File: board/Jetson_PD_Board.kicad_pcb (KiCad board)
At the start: 2 copper layers, 23.8 x 42.2 mm, 47 parts, among them J1 USB4081-03-A, J2 768250002, Q1 NTTFS5C673NLTAG, Q2 NTTFS5C673NLTAG, Q3 NTTFS5C673NLTAG, U1 APK43070DKZ-13-FA01, U2 USBLC6-2SC6

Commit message: Finished new layout before routing
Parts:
- moved D5 49.8 mm to (132.7, 79.8), turned to 180 degrees
- moved R12 49.6 mm to (129.5, 79.8), turned to 0 degrees
- moved U2 49.6 mm to (117.5, 105.8), turned to 0 degrees
- moved R1 47.3 mm to (129.4, 81.2), turned to 0 degrees
- moved C6 39.2 mm to (129.2, 99.0)
- moved R11 32.4 mm to (129.6, 105.8), turned to 0 degrees
- moved C9 31.2 mm to (121.5, 105.2)
- moved D4 30.6 mm to (132.8, 105.8), turned to 180 degrees
- moved R13 11.2 mm to (129.8, 92.0), turned to 90 degrees
- moved R16 6.57 mm to (123.2, 105.8)
- moved R17 6.57 mm to (125.0, 105.8)
- moved D1 4.69 mm to (121.5, 89.0), turned to 180 degrees
- moved C14 0.09 mm to (118.2, 99.0)
- moved R10 0.09 mm to (127.8, 92.0)
- moved R2 0.08 mm to (123.8, 92.0)
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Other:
- board size 23.8 x 42.2 mm -> 23.8 x 45.5 mm

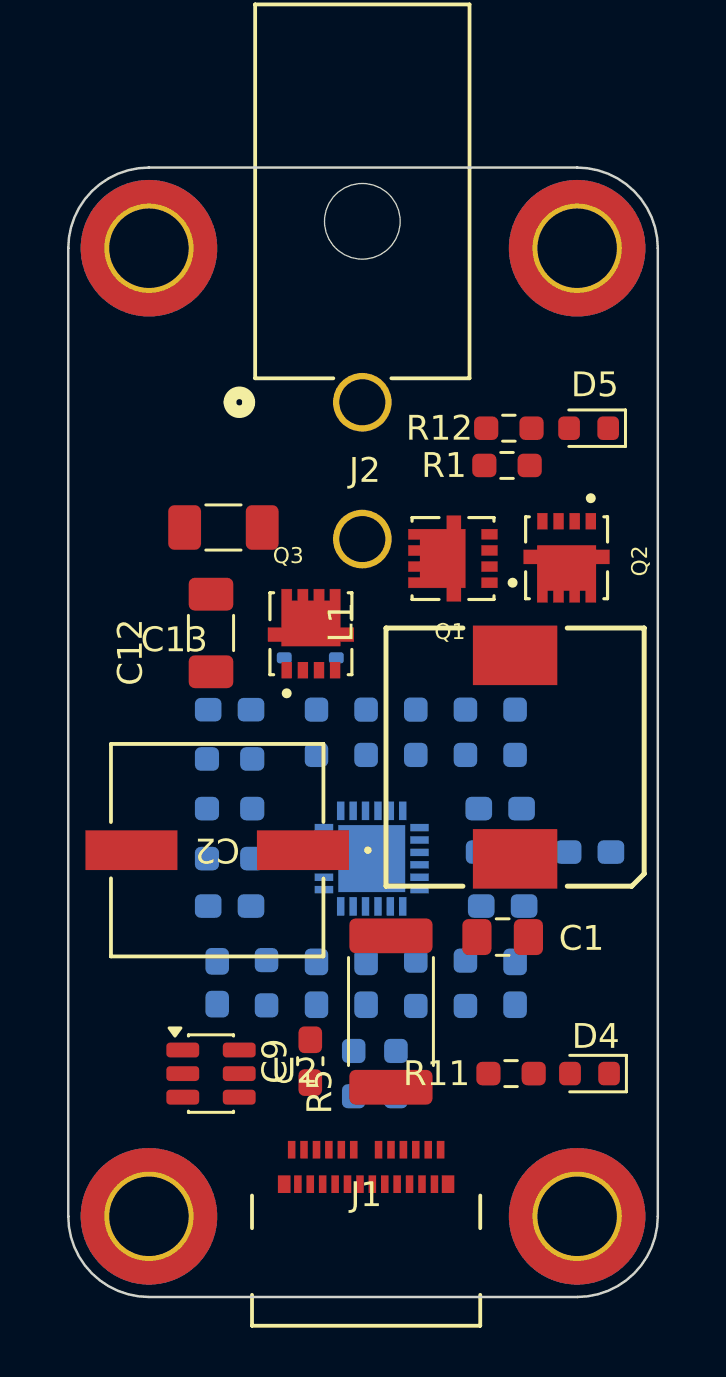
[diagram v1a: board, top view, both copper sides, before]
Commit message: Started routing power planes
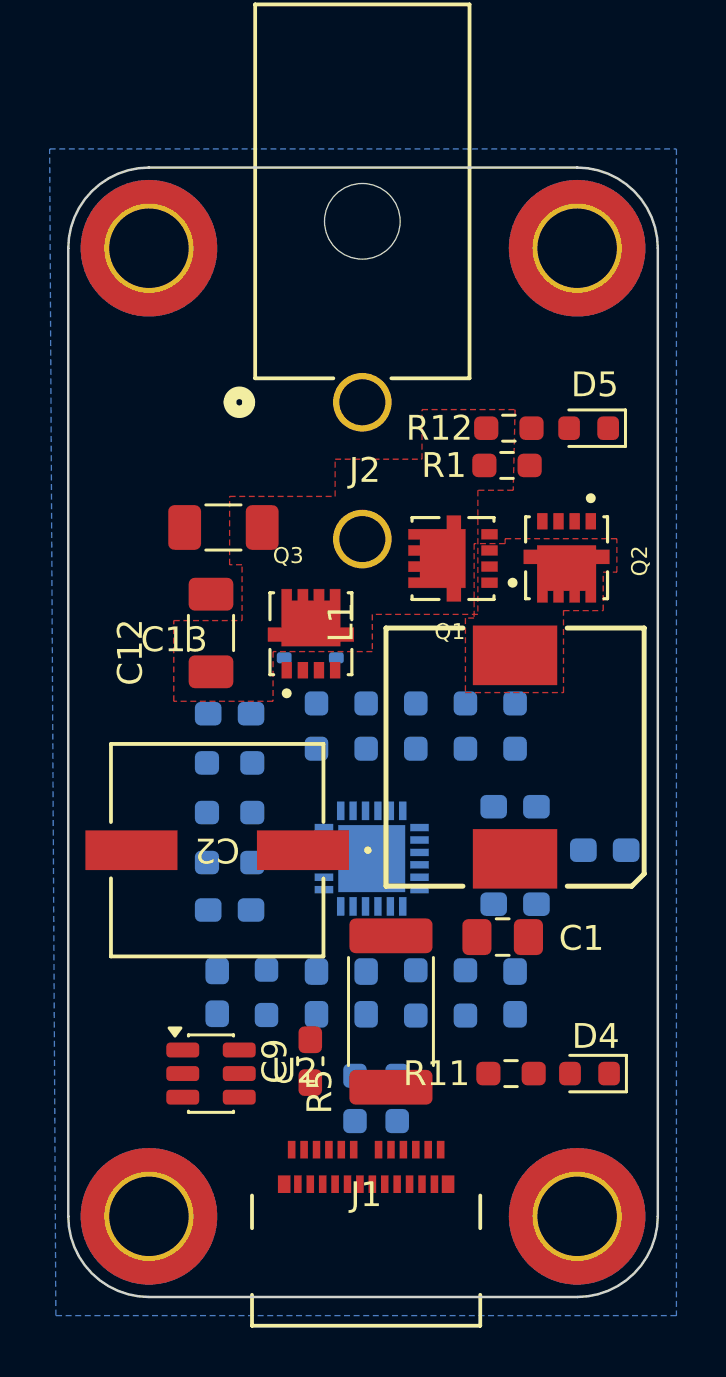
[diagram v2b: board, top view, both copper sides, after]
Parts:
- moved R16 1.00 mm to (123.3, 106.8)
- moved R17 1.00 mm to (125.0, 106.8)
- moved C3 0.62 mm to (133.4, 96.8)
- moved C4 0.60 mm to (129.8, 95.0)
- moved R4 0.59 mm to (129.8, 96.8)
- moved C6 0.51 mm to (129.8, 98.9)
- moved C10 0.39 mm to (121.8, 102.5)
- moved C5 0.39 mm to (117.8, 102.5)
- moved C7 0.39 mm to (129.8, 102.5)
- moved C8 0.39 mm to (123.8, 102.5)
- moved R3 0.39 mm to (119.7, 102.5)
- moved R6 0.39 mm to (125.8, 102.5)
- moved R7 0.39 mm to (127.8, 102.5)
- moved R10 0.25 mm to (127.8, 91.8)
- moved R13 0.25 mm to (129.8, 91.8)
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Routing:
- added copper zone on F.Cu, net /Switching_Node
- added copper zone on B.Cu, net GND
- added copper zone on F.Cu, net V_{batt}
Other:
- copper layers 2 -> 4

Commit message: aaaaaaaaaaaaaaaaaaaaaaaaA
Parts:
- C10: moved to F.Cu
- moved C10 9.09 mm to (129.5, 107.2), turned to 0 degrees
- moved C12 1.66 mm to (117.0, 86.4), turned to 180 degrees
- moved C13 1.42 mm to (118.8, 82.5), turned to 90 degrees
- moved C14 0.54 mm to (118.2, 99.7)
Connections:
- net Net-(D1-A) renamed /Buck_{out}
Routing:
- net Net-(Q2-G): track 0.00 -> 25.9 mm, vias 0 -> 2
- net Net-(U1-CC2): track 0.00 -> 23.1 mm
- net Net-(Q1-G): track 0.00 -> 20.9 mm, vias 0 -> 3
- net Net-(U1-CC1): track 0.00 -> 19.3 mm
- net Net-(U1-TS): track 0.00 -> 5.97 mm
- net CC2: track 0.00 -> 5.44 mm, vias 0 -> 1
- net Net-(U1-GPIO2): track 0.00 -> 4.70 mm
- net Net-(U1-DP): track 0.00 -> 3.34 mm
- net V_{batt}: track 0.00 -> 3.28 mm
- net Net-(U1-DN): track 0.00 -> 3.06 mm
- net Net-(D5-A): track 0.00 -> 3.04 mm
- net V_{out}: track 0.00 -> 2.98 mm
- net Net-(D4-A): track 0.00 -> 1.46 mm
- net GND: vias 0 -> 2
- added copper zone on F.Cu, net /Buck_{out}
- added copper zone on F.Cu, net GND
- added copper zone on F.Cu, net V_{out}

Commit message: Trace routing!
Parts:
- D1: moved to F.Cu
- moved R13 11.7 mm to (118.2, 89.5), turned to 0 degrees
- moved R6 10.7 mm to (122.0, 92.5)
- moved R7 10.7 mm to (124.0, 92.5)
- moved R3 10.3 mm to (130.0, 103.2)
- moved C5 10.3 mm to (128.0, 103.2)
- moved C7 5.74 mm to (124.0, 103.2)
- moved R2 4.27 mm to (128.0, 92.5)
- moved R8 4.27 mm to (126.0, 92.5)
- moved R10 4.27 mm to (131.9, 92.5)
- moved R9 4.27 mm to (129.9, 92.5)
- moved C14 3.84 mm to (121.5, 101.8), turned to -90 degrees
- moved C8 2.36 mm to (126.0, 103.2)
- moved D1 2.20 mm to (122.2, 91.1)
- moved D5 0.50 mm to (132.8, 80.2)
- moved R1 0.26 mm to (129.5, 81.0)
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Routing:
- net Net-(Q2-G): track 25.9 -> 0.00 mm, vias 2 -> 0
- net Net-(Q1-G): track 20.9 -> 0.00 mm, vias 3 -> 0
- net V_{batt}: track 3.28 -> 18.3 mm, vias 0 -> 1
- net Net-(U1-CC1): track 19.3 -> 11.1 mm
- net Net-(U1-CC2): track 23.1 -> 15.1 mm
- net Net-(D1-K): track 0.00 -> 5.34 mm, vias 0 -> 1
- net Net-(D5-A): track 3.04 -> 3.83 mm
- net GND: vias 2 -> 3

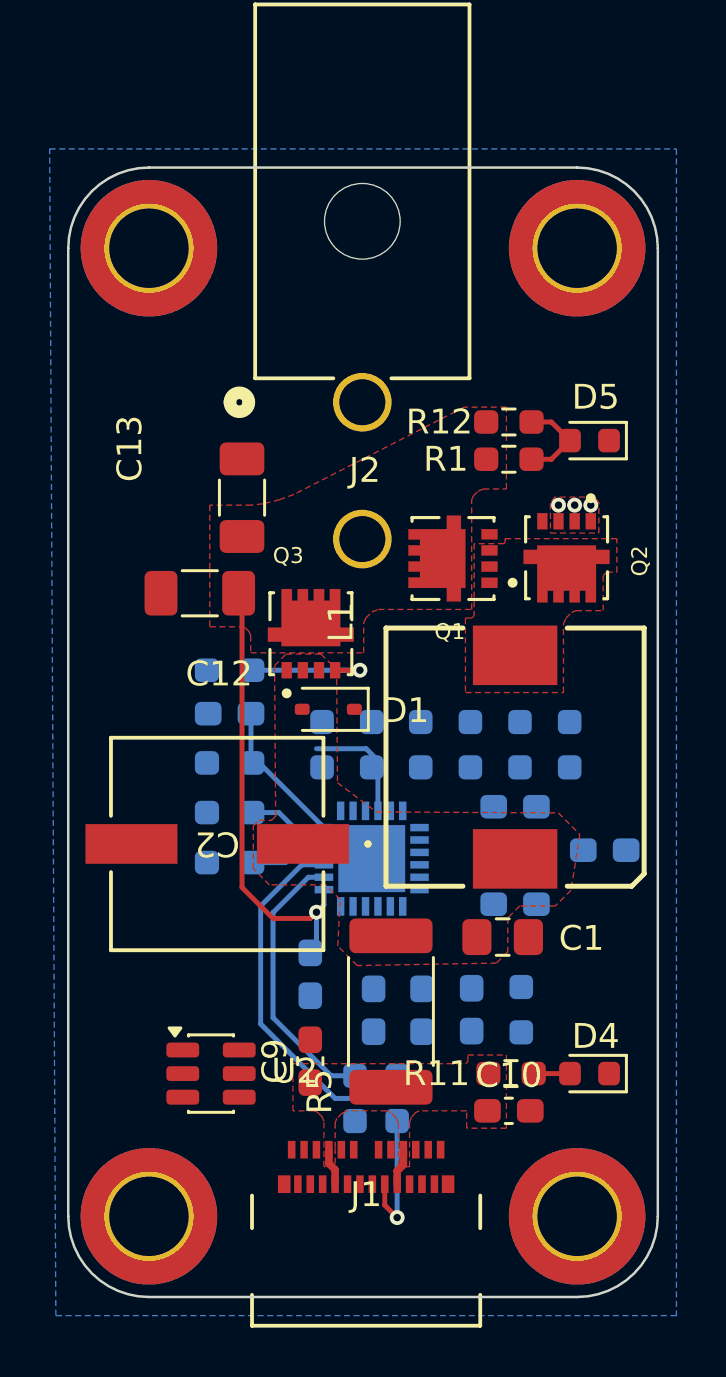
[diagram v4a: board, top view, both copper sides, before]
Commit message: Place components for a new arrangement for control IC
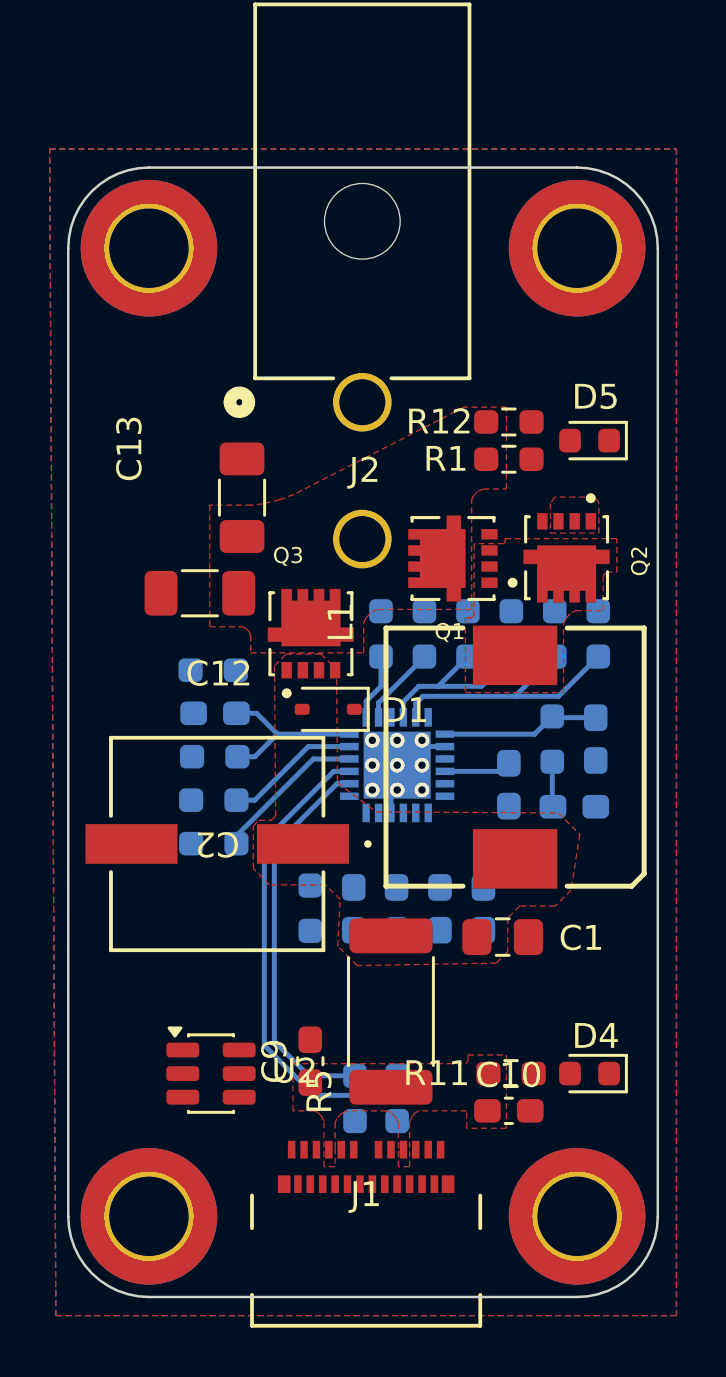
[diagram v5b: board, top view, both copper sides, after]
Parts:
- moved R3 9.43 mm to (121.5, 99.1)
- moved R6 5.06 mm to (124.3, 88.0)
- moved R7 4.94 mm to (126.1, 88.0)
- moved R8 4.85 mm to (127.8, 88.0)
- moved C6 4.82 mm to (129.5, 94.1), turned to -90 degrees
- moved R2 4.76 mm to (129.6, 88.0)
- moved R4 4.72 mm to (131.2, 92.3), turned to -90 degrees
- moved R9 4.68 mm to (131.3, 88.0)
- moved R10 4.61 mm to (133.1, 88.0)
- moved C4 4.24 mm to (133.0, 92.3), turned to -90 degrees
- moved C7 4.19 mm to (125.0, 99.1)
- moved C8 4.15 mm to (126.7, 99.1)
- moved C5 4.09 mm to (128.5, 99.1)
- moved U1 3.90 mm to (125.0, 93.3)
- moved C14 3.17 mm to (123.2, 99.1)
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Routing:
- net V_{batt}: track 18.3 -> 0.00 mm, vias 1 -> 0
- net Net-(U1-GPIO3): track 0.00 -> 11.0 mm
- net Net-(U1-COMP): track 0.00 -> 6.39 mm
- net CC2: track 5.44 -> 0.00 mm, vias 1 -> 0
- net Net-(D1-K): track 5.34 -> 0.00 mm, vias 1 -> 0
- net Net-(U1-CC1): track 11.1 -> 15.7 mm
- net Net-(U1-CC2): track 15.1 -> 19.3 mm
- net Net-(D5-A): track 3.83 -> 0.00 mm
- net Net-(U1-SCL): track 0.00 -> 3.22 mm
- net Net-(U1-DN): track 3.06 -> 6.14 mm
- net V_{out}: track 2.98 -> 0.00 mm
- net Net-(U1-GPIO2): track 4.70 -> 7.43 mm
- net /Switching_Node: track 0.00 -> 2.71 mm
- net Net-(U1-SDA): track 0.00 -> 2.70 mm
- net Net-(U1-DP): track 3.34 -> 5.44 mm
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- added copper zone on In1.Cu, net GND

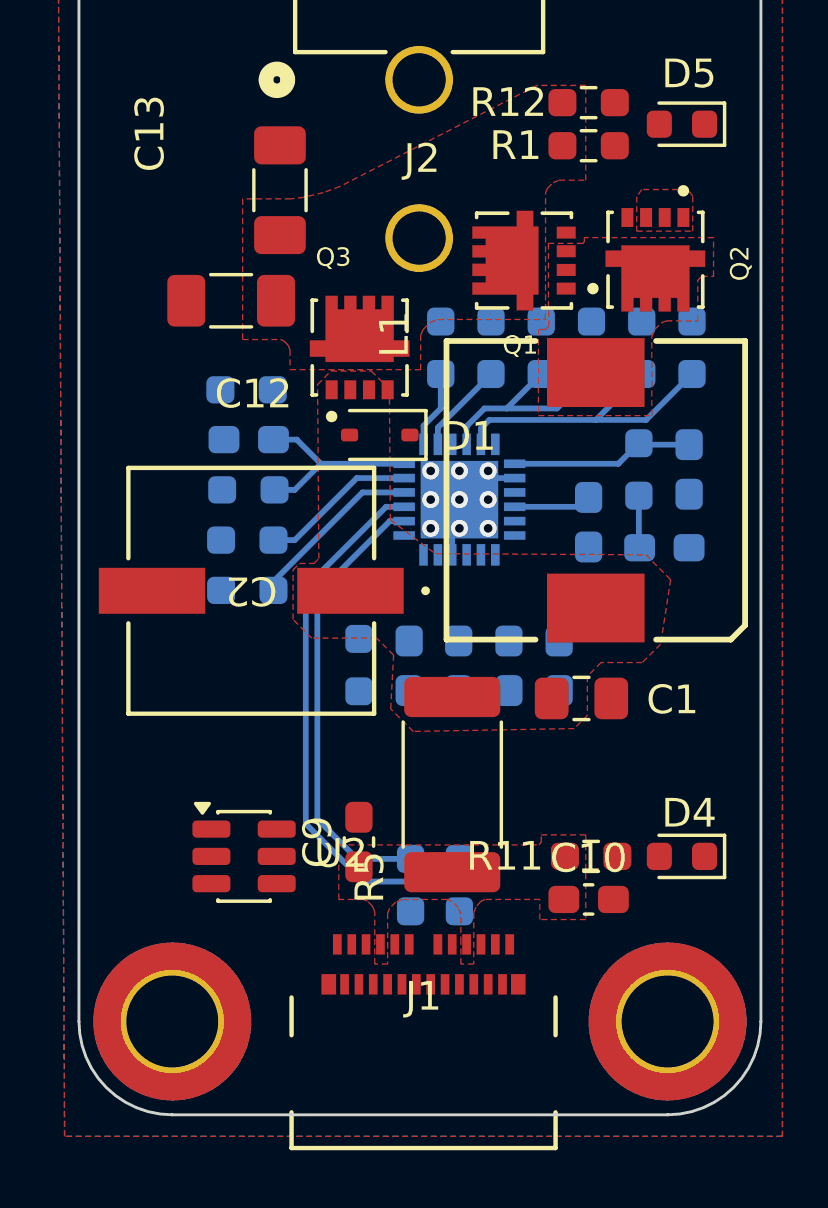
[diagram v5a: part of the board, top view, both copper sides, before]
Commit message: More trace routing
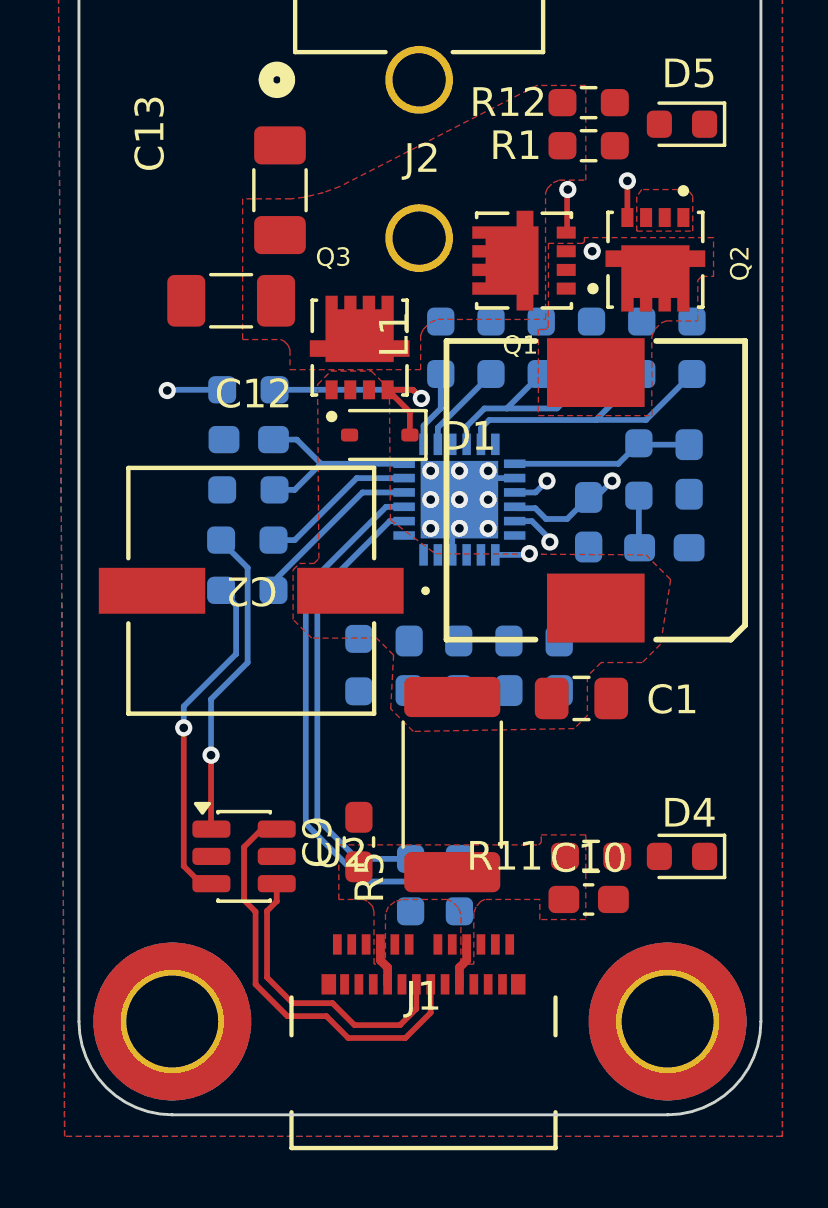
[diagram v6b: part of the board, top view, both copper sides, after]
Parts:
- moved R13 0.06 mm to (117.7, 89.5)
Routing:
- net Net-(Q1-G): track 0.00 -> 27.5 mm, vias 0 -> 2
- net /Switching_Node: track 2.71 -> 25.0 mm, vias 0 -> 2
- net Net-(U1-GATE): track 0.00 -> 20.5 mm, vias 0 -> 2
- net Net-(Q2-G): track 0.00 -> 20.4 mm, vias 0 -> 2
- net /USB_DP: track 0.00 -> 14.6 mm
- net /DN: track 0.00 -> 11.8 mm, vias 0 -> 1
- net /DP: track 0.00 -> 11.0 mm, vias 0 -> 1
- net /USB_DN: track 0.00 -> 10.4 mm
- net Net-(D1-K): track 0.00 -> 8.43 mm, vias 0 -> 1
- net V_{out}: track 0.00 -> 2.98 mm
- added copper zone on In2.Cu, net GND
- removed copper zone on In1.Cu, net GND
